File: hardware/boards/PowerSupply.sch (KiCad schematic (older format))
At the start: 72 parts, among them Q1 Q_NMOS_GSD, Q2 Q_NMOS_GSD, Q3 Q_NMOS_GSD, Q4 Q_NMOS_GSD, U2 ADP5050ACPZ-R7

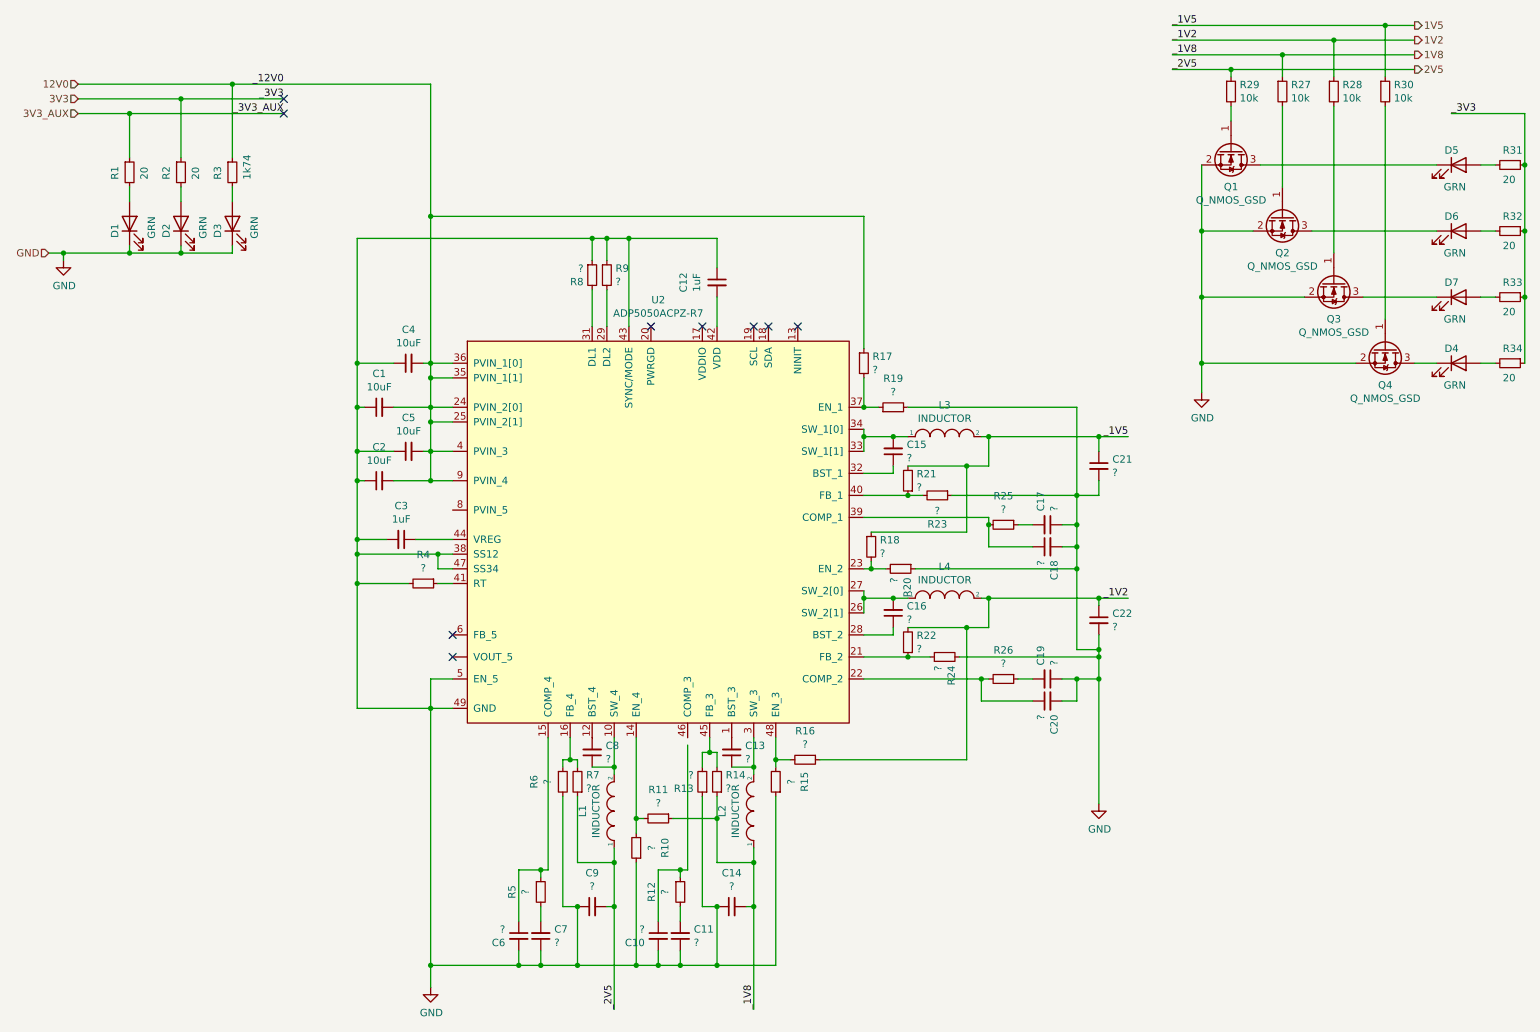
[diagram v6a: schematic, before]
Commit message: Updated the powersupply and schematic frames. Ran all the numbers for the passives for the supply
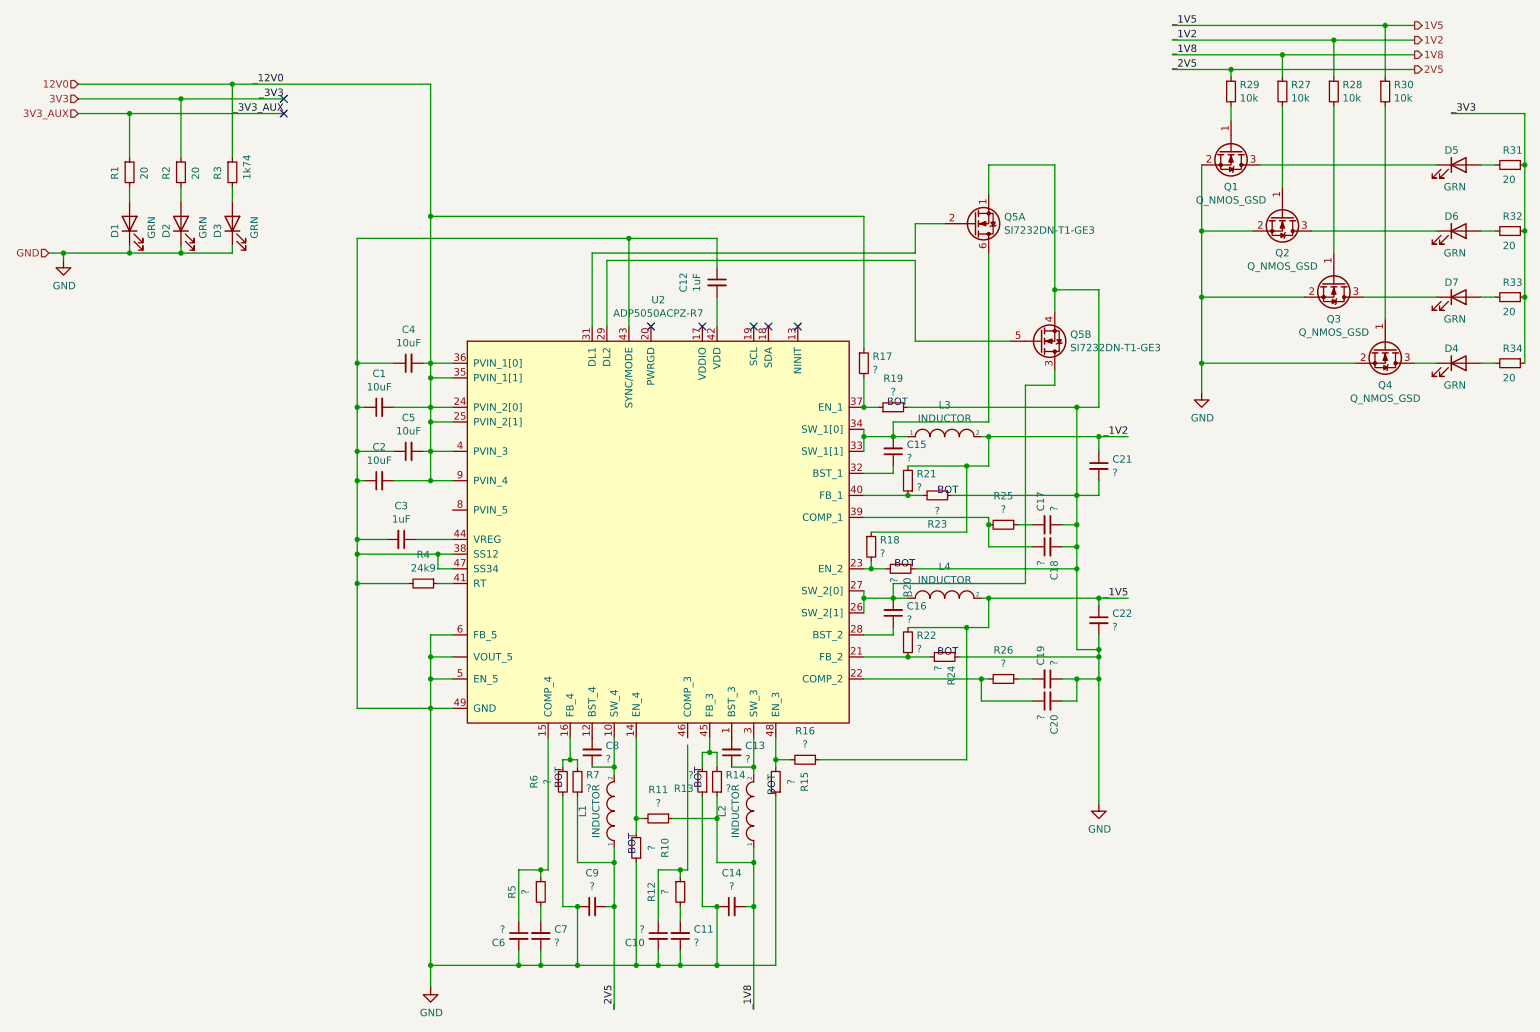
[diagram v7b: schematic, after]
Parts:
- removed R8, R9: ?, Resistor_SMD:R_0603_1608Metric, symbol Device:R_Small
- added Q5: SI7232DN-T1-GE3, lethalbit:Si7232DN, symbol Device:Q_DUAL_NMOS_S1G1D2S2G2D1
- L1, L2, L3, L4: footprint (none) -> Inductor_SMD:L_Coilcraft_XxL4040
- R4: value ? -> 24k9; MFR (none) -> Vishay Dale; MPN (none) -> CRCW060324K9FKEAC
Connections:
- net 1V2: now also C21.1, L3.2, R18.1, R21.2; no longer C22.1, L4.2, R16.1, R22.2
- net 1V5: now also C22.1, L4.2, R16.1, R22.2; no longer C21.1, L3.2, R18.1, R21.2
- net GND: now also U2.6 (FB_5), U2.~ (VOUT_5), Q5.1 (S), Q5.4 (S)
- net at C16.2, L4.1, U2.26 (SW_2[1])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: now also Q5.3 (D)
- net at U2.29 (DL2): now also Q5.5 (G)
- net at U2.31 (DL1): now also Q5.2 (G)
- net at C15.2, L3.1, U2.33 (SW_1[1])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: now also Q5.6 (D)
- no-connect marks 9 -> 7
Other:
- note added: "BOT\n"
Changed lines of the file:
@@
 encoding utf-8
 Sheet 5 10
-Title ""
-Date ""
-Rev ""
-Comp ""
+Title "lethallink - Power Supply"
+Date "2020-06-13"
+Rev "rev A"
+Comp "Aki Van Ness"
 Comment1 ""
 Comment2 ""
@@
 1V2
 $Comp
-L lethalbit:ADP5050ACPZ-R7 U2
-U 1 1 5ED78A27
-P 5250 4100
-F 0 "U2" H 5250 5731 50  0000 C CNN
-F 1 "ADP5050ACPZ-R7" H 5250 5640 50  0000 C CNN
-F 2 "lethalbit:QFN-48_EP_7x7_Pitch0.5mm" H 5250 4150 50  0001 C CNN
-F 3 "https://www.analog.com/media/en/technical-documentation/data-sheets/ADP5050.PDF" H 5250 4150 50  0001 C CNN
-F 4 "Analog Devices" H 5250 4100 50  0001 C CNN "MFR"
-F 5 " ADP5050ACPZ-R7 " H 5250 4100 50  0001 C CNN "MPN"
-	1    5250 4100
-	1    0    0    -1
-$EndComp
-$Comp
 L power:GND #PWR0110
 U 1 1 5ED7BA52
@@
 F 0 "L3" H 7200 3615 50  0000 C CNN
 F 1 "INDUCTOR" H 7200 3524 50  0000 C CNN
-F 2 "" H 7200 3400 50  0001 C CNN
+F 2 "Inductor_SMD:L_Coilcraft_XxL4040" H 7200 3400 50  0001 C CNN
 F 3 "~" H 7200 3400 50  0001 C CNN
 	1    7200 3400
@@
 F 0 "L2" H 5900 6165 50  0000 C CNN
 F 1 "INDUCTOR" H 5900 6074 50  0000 C CNN
-F 2 "" H 5900 5950 50  0001 C CNN
+F 2 "Inductor_SMD:L_Coilcraft_XxL4040" H 5900 5950 50  0001 C CNN
 F 3 "~" H 5900 5950 50  0001 C CNN
 	1    5900 5950
@@
 F 0 "L1" H 4950 6165 50  0000 C CNN
 F 1 "INDUCTOR" H 4950 6074 50  0000 C CNN
-F 2 "" H 4950 5950 50  0001 C CNN
+F 2 "Inductor_SMD:L_Coilcraft_XxL4040" H 4950 5950 50  0001 C CNN
 F 3 "~" H 4950 5950 50  0001 C CNN
 	1    4950 5950
@@
 	8250 4500 8250 4550
 Wire Wire Line
-	5900 5450 5900 5650
-Wire Wire Line
 	4950 5450 4950 5650
 Wire Wire Line
@@
 Wire Wire Line
 	8250 3400 8450 3400
+Text Label 8450 4500 2    50   ~ 0
+_1V5
 Text Label 8450 3400 2    50   ~ 0
-_1V5
-Text Label 8450 4500 2    50   ~ 0
 _1V2
 Text Label 4950 7300 1    50   ~ 0
@@
 Connection ~ 8250 4850
 $Comp
-L Device:R_Small R9
-U 1 1 5EE54CFB
-P 4900 2300
-F 0 "R9" H 4959 2346 50  0000 L CNN
-F 1 "?" H 4959 2255 50  0000 L CNN
-F 2 "Resistor_SMD:R_0603_1608Metric" H 4900 2300 50  0001 C CNN
-F 3 "~" H 4900 2300 50  0001 C CNN
-	1    4900 2300
-	1    0    0    -1
-$EndComp
-$Comp
-L Device:R_Small R8
-U 1 1 5EE575FF
-P 4800 2300
-F 0 "R8" H 4741 2254 50  0000 R CNN
-F 1 "?" H 4741 2345 50  0000 R CNN
-F 2 "Resistor_SMD:R_0603_1608Metric" H 4800 2300 50  0001 C CNN
-F 3 "~" H 4800 2300 50  0001 C CNN
-	1    4800 2300
-	1    0    0    -1
-$EndComp
-$Comp
 L Device:R_Small R4
 U 1 1 5EE5B1B8
 P 3650 4400
 F 0 "R4" V 3454 4400 50  0000 C CNN
-F 1 "?" V 3545 4400 50  0000 C CNN
+F 1 "24k9" V 3545 4400 50  0000 C CNN
 F 2 "Resistor_SMD:R_0603_1608Metric" H 3650 4400 50  0001 C CNN
 F 3 "~" H 3650 4400 50  0001 C CNN
+F 4 "Vishay Dale" V 3650 4400 50  0001 C CNN "MFR"
+F 5 "CRCW060324K9FKEAC" V 3650 4400 50  0001 C CNN "MPN"
 	1    3650 4400
 	0    1    1    0
@@
 	3200 4400 3200 5250
 Wire Wire Line
-	4900 2400 4900 2650
-Wire Wire Line
-	4800 2400 4800 2650
-Wire Wire Line
-	4800 2050 4800 2200
-Connection ~ 4800 2050
-Wire Wire Line
-	4800 2050 3200 2050
-Wire Wire Line
-	4900 2050 4900 2200
-Connection ~ 4900 2050
-Wire Wire Line
-	4900 2050 4800 2050
-Wire Wire Line
 	5050 2650 5050 2050
 Connection ~ 5050 2050
-Wire Wire Line
-	5050 2050 4900 2050
 $Comp
 L Device:R_Small R17
@@
 $EndComp
 Wire Wire Line
-	6650 3000 6650 3200
-Wire Wire Line
 	6650 3200 6750 3200
-Connection ~ 6650 3200
 Wire Wire Line
 	6950 3200 8100 3200
@@
 Connection ~ 6650 4500
 Wire Wire Line
-	6650 4500 6650 4600
-Wire Wire Line
 	6650 3350 6650 3400
 Connection ~ 6650 3400
-Wire Wire Line
-	6650 3400 6650 3500
 Connection ~ 8250 3400
 Wire Wire Line
@@
 F 0 "L4" H 7200 4715 50  0000 C CNN
 F 1 "INDUCTOR" H 7200 4624 50  0000 C CNN
-F 2 "" H 7200 4500 50  0001 C CNN
+F 2 "Inductor_SMD:L_Coilcraft_XxL4040" H 7200 4500 50  0001 C CNN
 F 3 "~" H 7200 4500 50  0001 C CNN
 	1    7200 4500
@@
 NoConn ~ 2700 1100
 NoConn ~ 2700 1200
-NoConn ~ 3850 4750
-NoConn ~ 3850 4900
 Wire Wire Line
 	3850 5050 3700 5050
@@
 	1    0    0    -1
 $EndComp
+Wire Wire Line
+	3850 4900 3700 4900
+Wire Wire Line
+	3700 4900 3700 5050
+Connection ~ 3700 5050
+Wire Wire Line
+	3850 4750 3700 4750
+Wire Wire Line
+	3700 4750 3700 4900
+Connection ~ 3700 4900
+Text Notes 7150 4900 0    50   ~ 0
+BOT\n
+Text Notes 7150 3800 0    50   ~ 0
+BOT\n
+Text Notes 5550 5800 1    50   ~ 0
+BOT\n
+Text Notes 4600 5800 1    50   ~ 0
+BOT\n
+Text Notes 5100 6250 1    50   ~ 0
+BOT\n
+Text Notes 6050 5850 1    50   ~ 0
+BOT\n
+Text Notes 7000 4300 2    50   ~ 0
+BOT\n
+Text Notes 6950 3200 2    50   ~ 0
+BOT\n
+Wire Wire Line
+	3200 2050 5050 2050
+Connection ~ 6650 3200
+Wire Wire Line
+	6650 4500 6650 4600
+Wire Wire Line
+	6650 3400 6650 3500
+Wire Wire Line
+	6650 3000 6650 3200
+Wire Wire Line
+	5900 5450 5900 5650
+$Comp
+L lethalbit:ADP5050ACPZ-R7 U2
+U 1 1 5ED78A27
+P 5250 4100
+F 0 "U2" H 5250 5731 50  0000 C CNN
+F 1 "ADP5050ACPZ-R7" H 5250 5640 50  0000 C CNN
+F 2 "lethalbit:QFN-48_EP_7x7_Pitch0.5mm" H 5250 4150 50  0001 C CNN
+F 3 "https://www.analog.com/media/en/technical-documentation/data-sheets/ADP5050.PDF" H 5250 4150 50  0001 C CNN
+F 4 "Analog Devices" H 5250 4100 50  0001 C CNN "MFR"
+F 5 " ADP5050ACPZ-R7 " H 5250 4100 50  0001 C CNN "MPN"
+	1    5250 4100
+	1    0    0    -1
+$EndComp
+$Comp
+L Device:Q_DUAL_NMOS_S1G1D2S2G2D1 Q5
+U 2 1 5EF3AC59
+P 7850 2750
+F 0 "Q5" H 8055 2704 50  0000 L CNN
+F 1 "SI7232DN-T1-GE3" H 8055 2795 50  0000 L CNN
+F 2 "lethalbit:Si7232DN" H 8050 2750 50  0001 C CNN
+F 3 "https://www.vishay.com/docs/68986/si7232dn.pdf" H 8050 2750 50  0001 C CNN
+F 4 "Vishay Siliconix" H 7850 2750 50  0001 C CNN "MFR"
+F 5 "SI7232DN-T1-GE3" H 7850 2750 50  0001 C CNN "MPN"
+	2    7850 2750
+	1    0    0    1
+$EndComp
+$Comp
+L Device:Q_DUAL_NMOS_S1G1D2S2G2D1 Q5
+U 1 1 5EF3BA04
+P 7400 1950
+F 0 "Q5" H 7605 1904 50  0000 L CNN
+F 1 "SI7232DN-T1-GE3" H 7605 1995 50  0000 L CNN
+F 2 "lethalbit:Si7232DN" H 7600 1950 50  0001 C CNN
+F 3 "https://www.vishay.com/docs/68986/si7232dn.pdf" H 7600 1950 50  0001 C CNN
+F 4 "Vishay Siliconix" H 7400 1950 50  0001 C CNN "MFR"
+F 5 "SI7232DN-T1-GE3" H 7400 1950 50  0001 C CNN "MPN"
+	1    7400 1950
+	1    0    0    1
+$EndComp
+Wire Wire Line
+	7500 1750 7500 1550
+Wire Wire Line
+	7500 1550 7950 1550
+Wire Wire Line
+	7950 1550 7950 2400
+Wire Wire Line
+	7950 2400 8250 2400
+Wire Wire Line
+	8250 2400 8250 3200
+Wire Wire Line
+	8250 3200 8100 3200
+Connection ~ 7950 2400
+Wire Wire Line
+	7950 2400 7950 2550
+Connection ~ 8100 3200
+Wire Wire Line
+	4900 2650 4900 2200
+Wire Wire Line
+	4900 2200 7000 2200
+Wire Wire Line
+	7000 2200 7000 2750
+Wire Wire Line
+	7000 2750 7650 2750
+Wire Wire Line
+	4800 2650 4800 2150
+Wire Wire Line
+	4800 2150 7000 2150
+Wire Wire Line
+	7000 2150 7000 1950
+Wire Wire Line
+	7000 1950 7200 1950
+Wire Wire Line
+	6850 3400 6850 3300
+Wire Wire Line
+	6850 3300 7500 3300
+Wire Wire Line
+	7500 3300 7500 2150
+Wire Wire Line
+	6850 4500 6850 4400
+Wire Wire Line
+	6850 4400 7750 4400
+Wire Wire Line
+	7750 4400 7750 3050
+Wire Wire Line
+	7750 3050 7950 3050
+Wire Wire Line
+	7950 3050 7950 2950
 $EndSCHEMATC

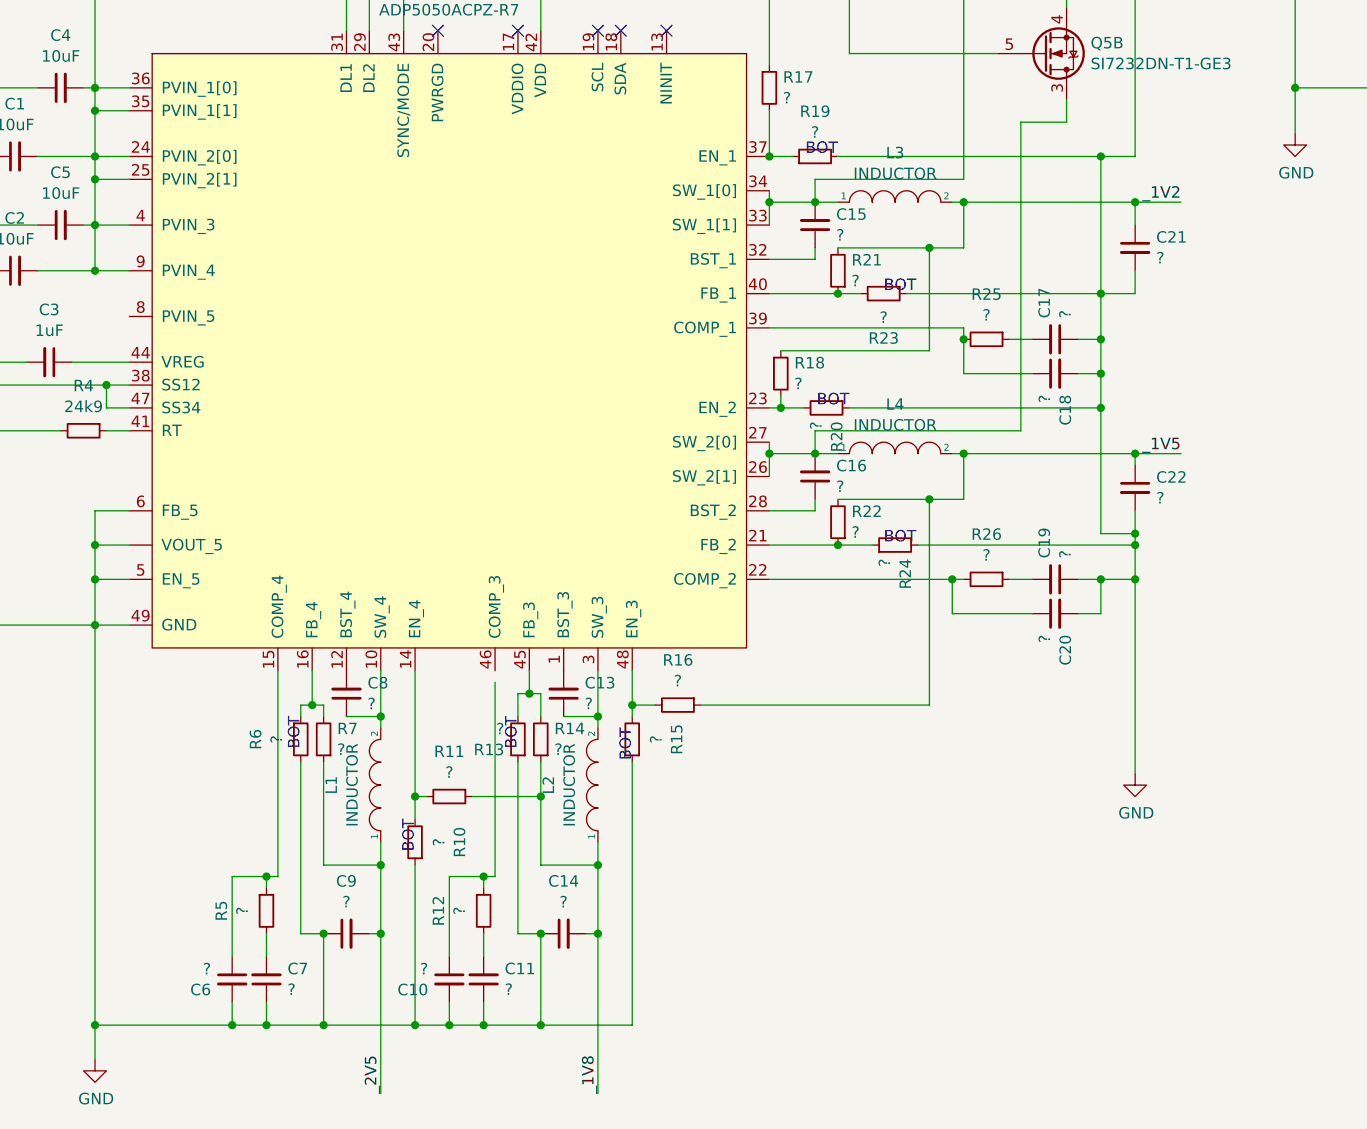
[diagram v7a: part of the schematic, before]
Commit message: Populated most of the values for the powersupply
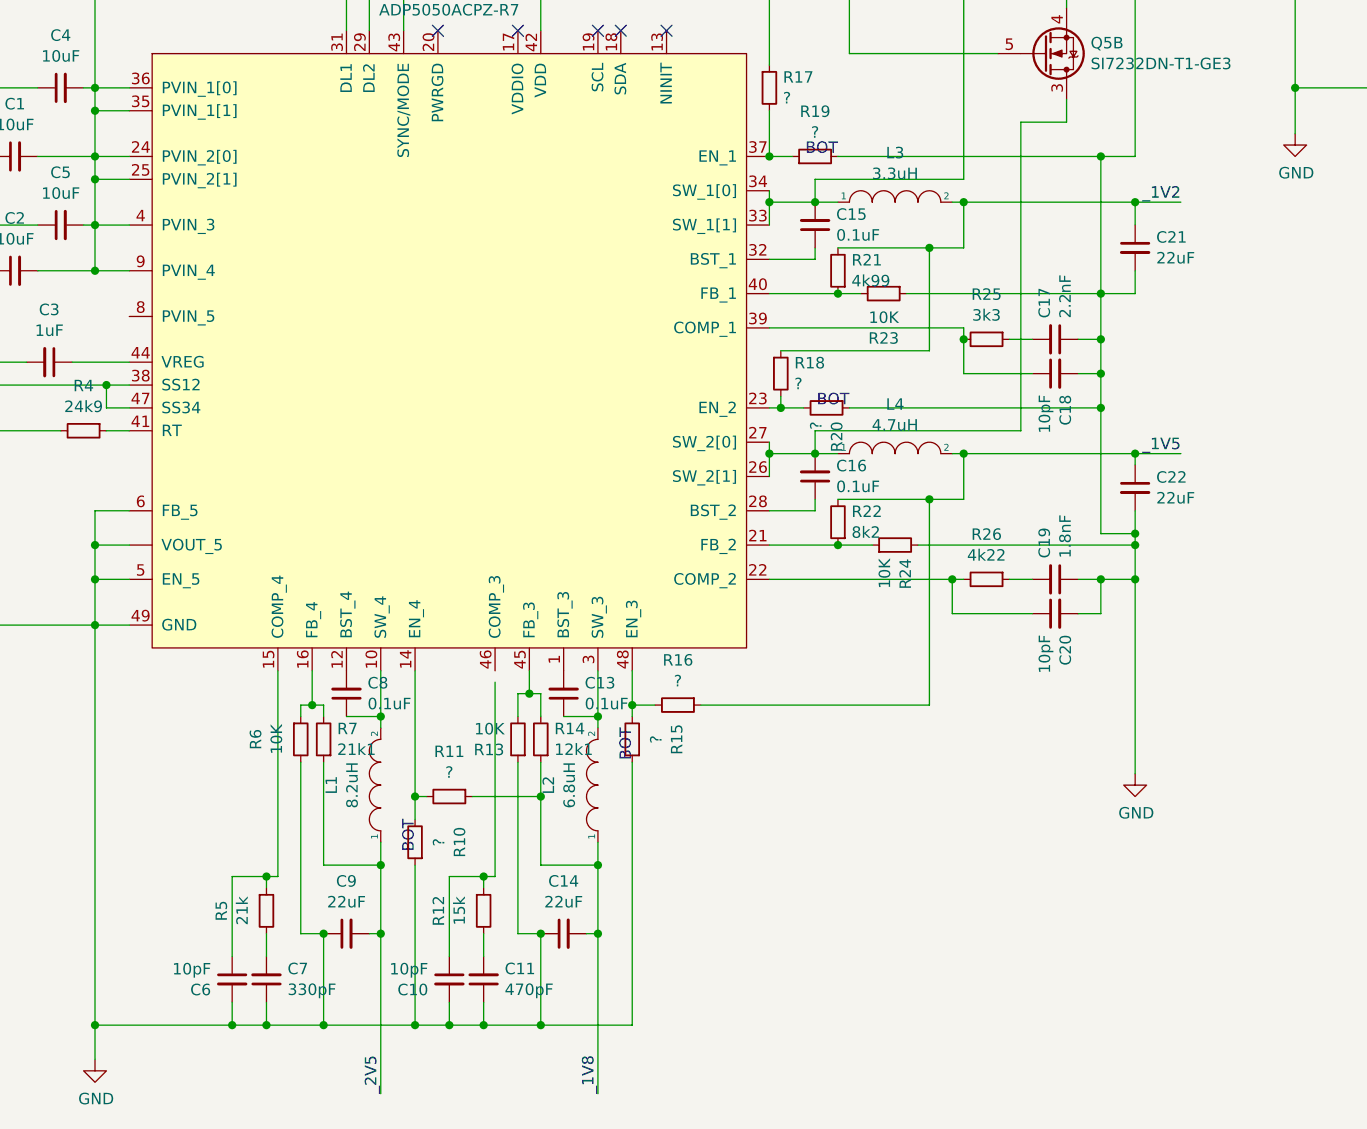
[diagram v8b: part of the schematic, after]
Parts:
- C10, C18, C20, C6: value ? -> 10pF; MPN (none) -> C0603C100K5RAC7867
- C11: value ? -> 470pF; MPN (none) -> C0603C471J5RACTU
- C13, C16, C8: value ? -> 0.1uF; MPN C0603C105K4RACTU -> C0603C104M5RACTU
- C14, C21, C22, C9: value ? -> 22uF; MFR (none) -> KEMET; MPN (none) -> C1206C226K9PACTU
- C15: value ? -> 0.1uF; MPN (none) -> C0603C104M5RACTU
- C17: value ? -> 2.2nF; MPN (none) -> C0603C222J3RACTU
- C19: value ? -> 1.8nF; MPN (none) -> C0603C182J5RACTU
- C7: value ? -> 330pF; MPN (none) -> C0603C331J5RACTU
- L1: value INDUCTOR -> 8.2uH; MFR (none) -> Coilcraft; MPN (none) -> XAL4040-822MEC
- L2: value INDUCTOR -> 6.8uH; footprint Inductor_SMD:L_Coilcraft_XxL4040 -> Inductor_SMD:L_Coilcraft_XxL4030; MFR (none) -> Coilcraft; MPN (none) -> XAL4030-682MEC
- L3: value INDUCTOR -> 3.3uH; footprint Inductor_SMD:L_Coilcraft_XxL4040 -> Inductor_SMD:L_Coilcraft_XxL4020; MFR (none) -> Coilcraft; MPN (none) -> XFL4020-332MEC
- L4: value INDUCTOR -> 4.7uH; footprint Inductor_SMD:L_Coilcraft_XxL4040 -> Inductor_SMD:L_Coilcraft_XxL4020; MFR (none) -> Coilcraft; MPN (none) -> XFL4020-472MEC
- R12: value ? -> 15k; MFR (none) -> Vishay Dale; MPN (none) -> CRCW060315K0FKEAHP
- R13, R23, R24, R6: value ? -> 10K; MFR (none) -> Vishay Dale; MPN (none) -> RCS060310K0FKEA
- R14: value ? -> 12k1; MFR (none) -> Vishay Dale; MPN (none) -> CRCW060312K1FKEAHP
- R21: value ? -> 4k99; MFR (none) -> Vishay Dale; MPN (none) -> RCS06034K99FKEA
- R22: value ? -> 8k2; MFR (none) -> Vishay Dale; MPN (none) -> RCS06038K20FKEA
- R25: value ? -> 3k3; MFR (none) -> Vishay Dale; MPN (none) -> CRCW06033K30FKEAHP
- R26: value ? -> 4k22; Field5 (none) -> CRCW06034K22FKEAHP; MFR (none) -> Vishay Dale
- R5: value ? -> 21k; MFR (none) -> Vishay Dale; MPN (none) -> CRCW060321K0FKEAHP
- R7: value ? -> 21k1; MFR (none) -> Vishay Dale; MPN (none) -> CRCW060322K1FKEAHP
